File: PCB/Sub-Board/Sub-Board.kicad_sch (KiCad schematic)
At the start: 0 parts

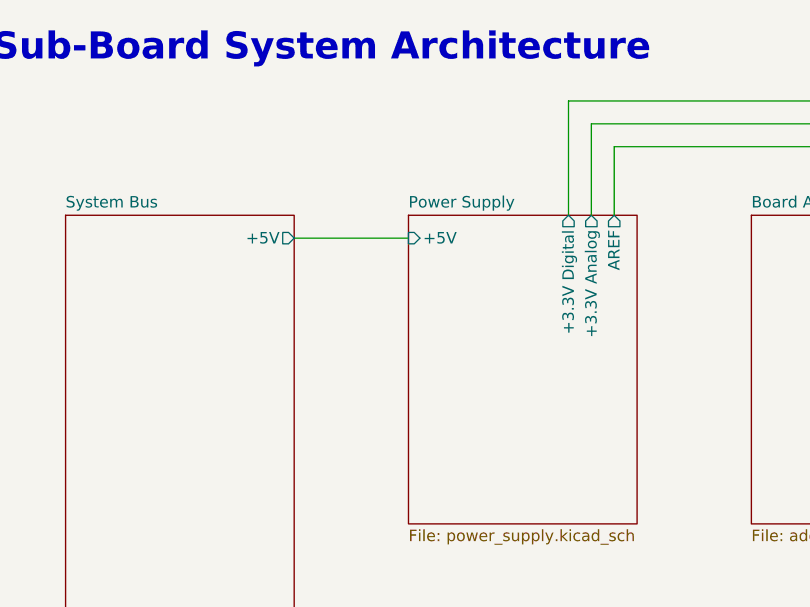
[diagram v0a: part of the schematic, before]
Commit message: Sub-Board PCB before ERC
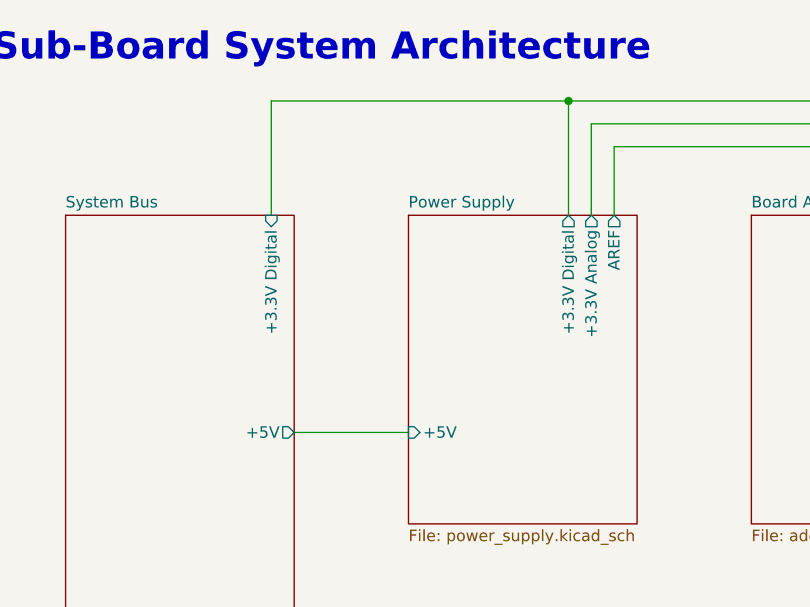
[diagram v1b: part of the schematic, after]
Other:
- sheet System Bus ports: added +3.3V Digital; removed none
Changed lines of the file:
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@@
+	)
+	(junction
+		(at 81.28 25.4)
+		(diameter 0)
+		(color 0 0 0 0)
 	)
 	(junction
@@
 	(wire
 		(pts
-			(xy 50.8 40.64) (xy 63.5 40.64)
+			(xy 50.8 62.23) (xy 63.5 62.23)
 		)
 		(stroke
@@
 	(wire
 		(pts
+			(xy 48.26 25.4) (xy 81.28 25.4)
+		)
+		(stroke
+			(width 0)
+			(type default)
+		)
+	)
+	(wire
+		(pts
 			(xy 213.36 30.48) (xy 213.36 38.1)
 		)
@@
 		(pts
 			(xy 124.46 25.4) (xy 170.18 25.4)
+		)
+		(stroke
+			(width 0)
+			(type default)
+		)
+	)
+	(wire
+		(pts
+			(xy 48.26 38.1) (xy 48.26 25.4)
 		)
 		(stroke
@@
 		)
 		(pin "+5V" input
-			(at 63.5 40.64 180)
+			(at 63.5 62.23 180)
 			(effects
 				(font
@@
 		)
 		(pin "+5V" output
-			(at 50.8 40.64 0)
+			(at 50.8 62.23 0)
 			(effects
 				(font
@@
 			(effects
 				(font
+					(size 1.27 1.27)
+				)
+				(justify right)
+			)
+		)
+		(pin "+3.3V Digital" input
+			(at 48.26 38.1 90)
+			(effects
+				(font

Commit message: Sub-Board PCB after ERC
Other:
- sheet Board Address ports: added BoardAddress[0..7]; removed BoardAddress
- sheet STM32-MCU ports: added BoardAddress[0..7], Slot0{Slot}, Slot1{Slot}, Slot2{Slot}, Slot3{Slot}, Slot4{Slot}, Slot5{Slot}, Slot6{Slot}, Slot7{Slot}; removed BoardAddress, Slot(0), Slot(1), Slot(2), Slot(3), Slot(4), Slot(5), Slot(6), Slot(7)
- sheet Slots ports: added Slot0{Slot}, Slot1{Slot}, Slot2{Slot}, Slot3{Slot}, Slot4{Slot}, Slot5{Slot}, Slot6{Slot}, Slot7{Slot}; removed Slot(0), Slot(1), Slot(2), Slot(3), Slot(4), Slot(5), Slot(6), Slot(7)
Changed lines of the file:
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@@
 			)
 		)
-		(pin "BoardAddress" output
+		(pin "BoardAddress[0..7]" output
 			(at 127 62.23 0)
 			(effects
@@
 			)
 		)
-		(pin "Slot(0)" bidirectional
+		(pin "Slot0{Slot}" bidirectional
 			(at 190.5 62.23 180)
 			(effects
@@
 			)
 		)
-		(pin "Slot(6)" bidirectional
+		(pin "Slot6{Slot}" bidirectional
 			(at 190.5 77.47 180)
 			(effects
@@
 			)
 		)
-		(pin "Slot(4)" bidirectional
+		(pin "Slot4{Slot}" bidirectional
 			(at 190.5 72.39 180)
 			(effects
@@
 			)
 		)
-		(pin "Slot(5)" bidirectional
+		(pin "Slot5{Slot}" bidirectional
 			(at 190.5 74.93 180)
 			(effects
@@
 			)
 		)
-		(pin "Slot(2)" bidirectional
+		(pin "Slot2{Slot}" bidirectional
 			(at 190.5 67.31 180)
 			(effects
@@
 			)
 		)
-		(pin "Slot(3)" bidirectional
+		(pin "Slot3{Slot}" bidirectional
 			(at 190.5 69.85 180)
 			(effects
@@
 			)
 		)
-		(pin "Slot(7)" bidirectional
+		(pin "Slot7{Slot}" bidirectional
 			(at 190.5 80.01 180)
 			(effects
@@
 			)
 		)
-		(pin "Slot(1)" bidirectional
+		(pin "Slot1{Slot}" bidirectional
 			(at 190.5 64.77 180)
 			(effects
@@
 			)
 		)
-		(pin "Slot(2)" bidirectional
+		(pin "Slot2{Slot}" bidirectional
 			(at 177.8 67.31 0)
 			(effects
@@
 			)
 		)
-		(pin "Slot(0)" bidirectional
+		(pin "Slot0{Slot}" bidirectional
 			(at 177.8 62.23 0)
 			(effects
@@
 			)
 		)
-		(pin "Slot(3)" bidirectional
+		(pin "Slot3{Slot}" bidirectional
 			(at 177.8 69.85 0)
 			(effects
@@
 			)
 		)
-		(pin "Slot(1)" bidirectional
+		(pin "Slot1{Slot}" bidirectional
 			(at 177.8 64.77 0)
 			(effects
@@
 			)
 		)
-		(pin "Slot(5)" bidirectional
+		(pin "Slot5{Slot}" bidirectional
 			(at 177.8 74.93 0)
 			(effects
@@
 			)
 		)
-		(pin "Slot(4)" bidirectional
+		(pin "Slot4{Slot}" bidirectional
 			(at 177.8 72.39 0)
 			(effects
@@
 			)
 		)
-		(pin "Slot(6)" bidirectional
+		(pin "Slot6{Slot}" bidirectional
 			(at 177.8 77.47 0)
 			(effects
@@
 			)
 		)
-		(pin "Slot(7)" bidirectional
+		(pin "Slot7{Slot}" bidirectional
 			(at 177.8 80.01 0)
 			(effects
@@
 			)
 		)
-		(pin "BoardAddress" input
+		(pin "BoardAddress[0..7]" input
 			(at 139.7 62.23 180)
 			(effects

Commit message: Sub-Board PCB: I2C Busses
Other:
- sheet STM32-MCU ports: added SlotBus{I2C}, SystemBus{I2C}; removed SlotBus.Clock, SlotBus.Data, SystemBus.Clock, SystemBus.Data
- sheet Slots ports: added SlotBus{I2C}; removed SlotBus.Clock, SlotBus.Data
- sheet System Bus ports: added SystemBus{I2C}; removed SystemBus.Clock, SystemBus.Data

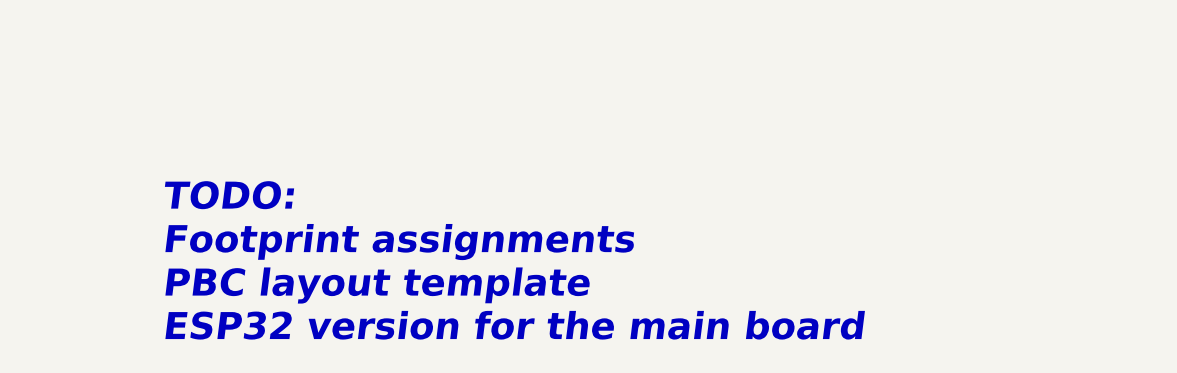
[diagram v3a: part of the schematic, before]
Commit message: Sub-Board PCB: Footprint assignments
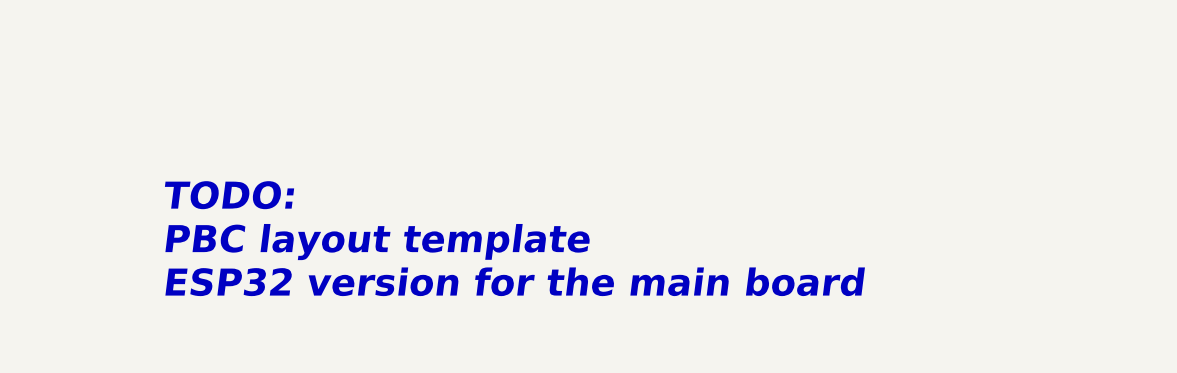
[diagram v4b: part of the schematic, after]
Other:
- note added: "TODO: PBC layout template ESP32 version for the main board"
- note removed: "TODO: Footprint assignments PBC layout template ESP32 version for the main board"
- title: Modular Music Controller – Template -> Modular Music Controller / Sub-Board / Architecture
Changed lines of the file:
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@@
 	(paper "A4")
 	(title_block
-		(title "Modular Music Controller – Template")
+		(title "Modular Music Controller / Sub-Board / Architecture")
 		(date "2025-11-01")
 		(rev "1")
@@
 		)
 	)
-	(text "TODO:\nFootprint assignments\nPBC layout template\nESP32 version for the main board"
+	(text "TODO:\nPBC layout template\nESP32 version for the main board"
 		(exclude_from_sim no)
 		(at 44.196 120.396 0)

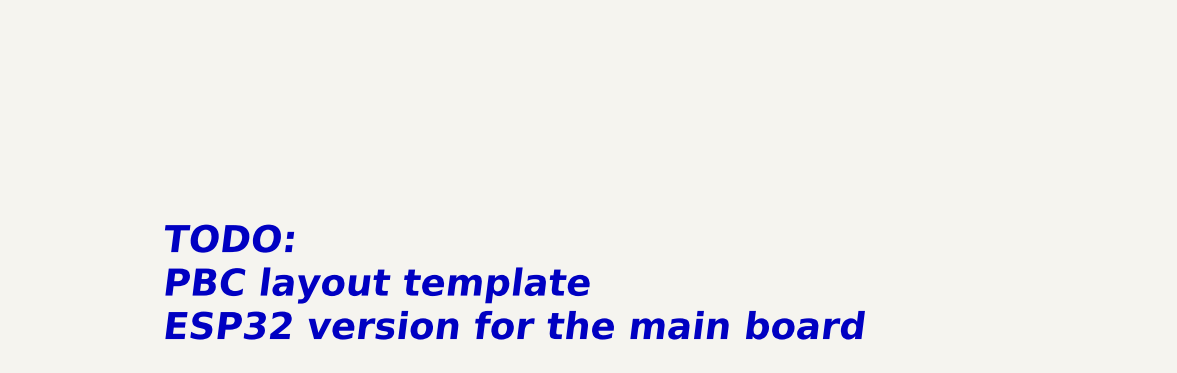
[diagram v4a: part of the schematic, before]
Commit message: Sub Board PCB: Pin Connectors
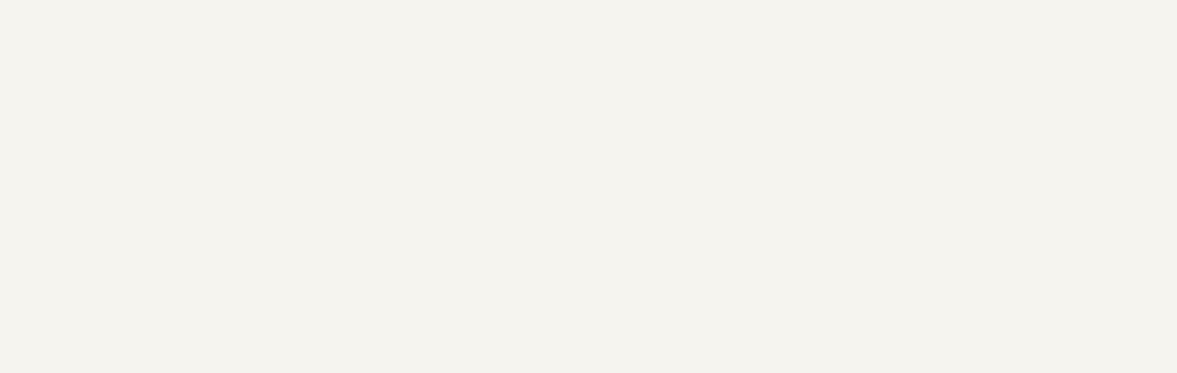
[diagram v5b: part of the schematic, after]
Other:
- note removed: "TODO: PBC layout template ESP32 version for the main board"
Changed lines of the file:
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@@
-		)
-	)
-	(text "TODO:\nPBC layout template\nESP32 version for the main board"
-		(exclude_from_sim no)
-		(at 44.196 120.396 0)
-		(effects
-			(font
-				(size 3 3)
-				(thickness 0.254)
-				(bold yes)
-				(italic yes)
-			)
-			(justify left top)
 		)
 	)
